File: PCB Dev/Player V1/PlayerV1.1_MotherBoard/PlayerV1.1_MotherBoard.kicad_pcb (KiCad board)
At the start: 2 copper layers, 64.3 x 83.5 mm, 66 parts, among them J1 USB_C_Receptacle_USB2.0, J3 SJ-3524-SMT-BE, U1 MIC5213-2.5YC5-TR, U2 TP4056, U3 AP7217A, U4 CP2102N-A02-GQFN28R, U5 BQ27441DRZR-G1A, U6 ESP32-WROOM-32E_(16MB), U7 MCP23017-E/ML

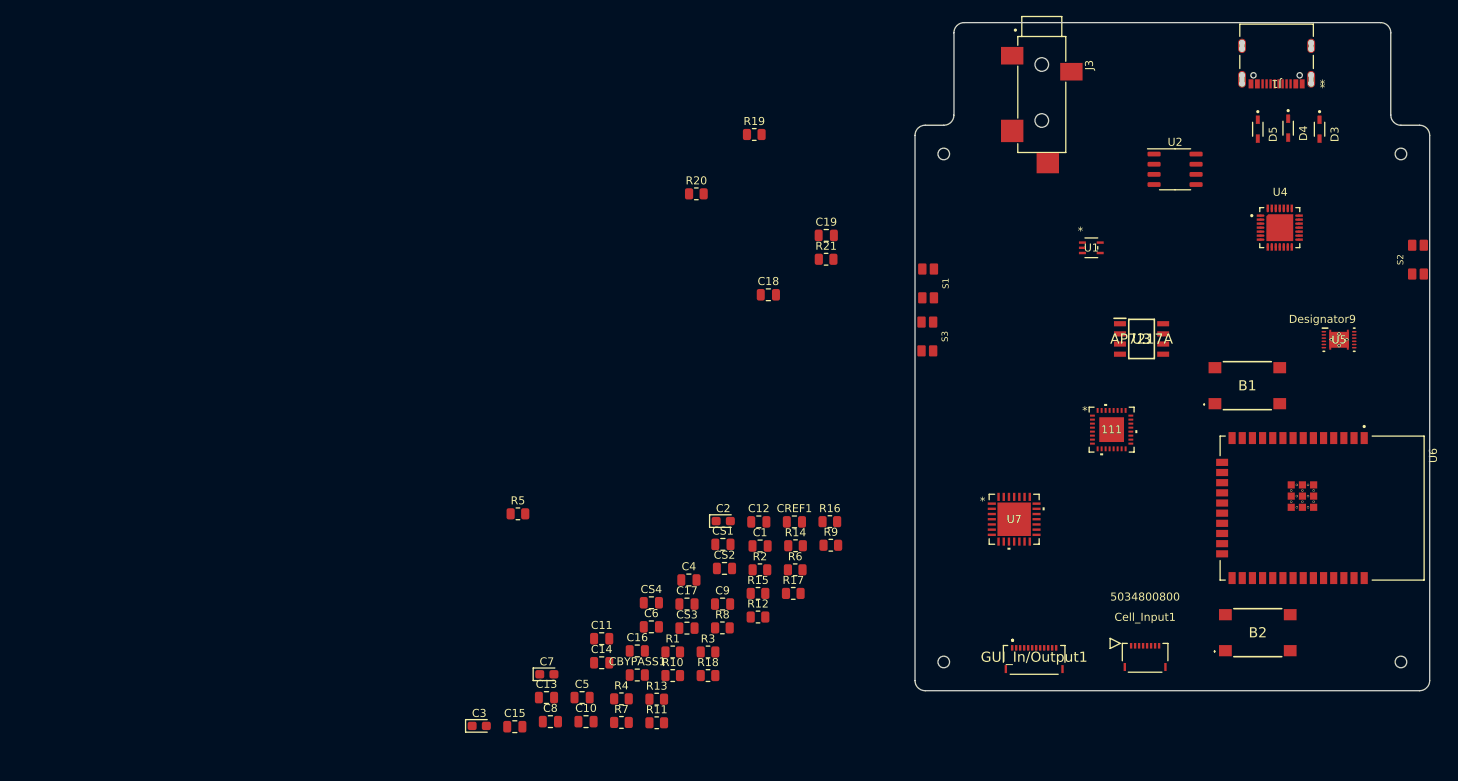
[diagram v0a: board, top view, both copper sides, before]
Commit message: added all jst connectors
new upward facing jst connectors
fixed footprint issue on the usbC port that resulted in a malformed board outline
need to add holes for the usbc port somehow
need to start laying out the pcb after using the component measurements to make proper pcb heights, cutouts, and tactile buttons
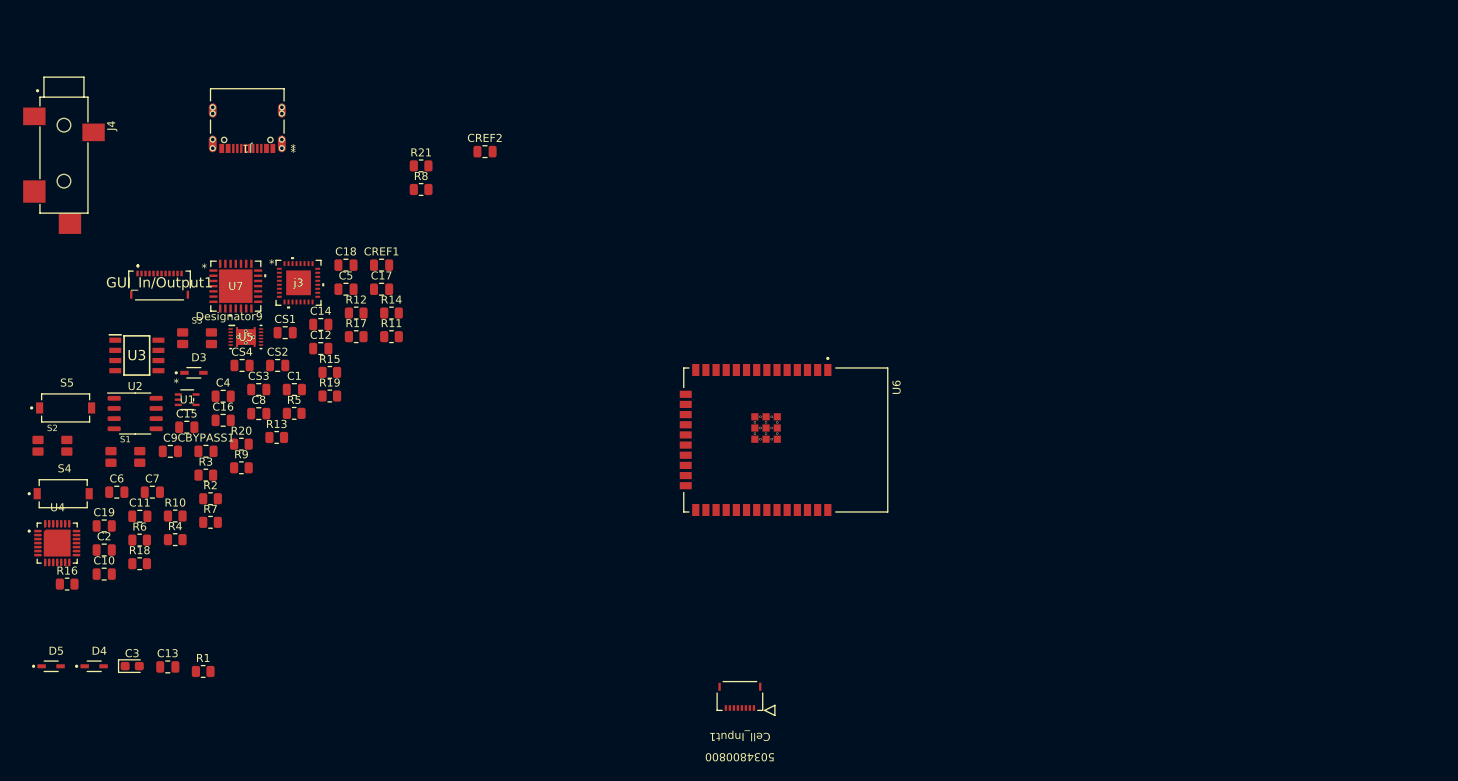
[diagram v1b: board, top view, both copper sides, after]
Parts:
- removed 111: LM49450SQ_NOPB, LM49450SQ_NOPB:SQA32A
- removed B1, B2: EVP-BT7A4A000, EVP-BT7A4A000:EVPBT7A4A000
- removed J3: SJ-3524-SMT-BE, SJ-3524-SMT-BE:CUI_SJ-3524-SMT-BE
- added CREF2: 0.1uF, Capacitor_SMD:C_0805_2012Metric, F.Cu at (110.9, 58.0)
- added J4: SJ-3524-SMT-BE, SJ-3524-SMT-BE:CUI_SJ-3524-SMT-BE, F.Cu at (58.2, 54.7)
- added S4: PTS636, PTS636_SM43J_SMTR_LFS:SW_PTS636_SM43J_SMTR_LFS, F.Cu at (58.1, 100.8)
- added S5: PTS636, PTS636_SM43J_SMTR_LFS:SW_PTS636_SM43J_SMTR_LFS, F.Cu at (58.4, 90.1)
- added j3: LM49450SQ_NOPB, LM49450SQ_NOPB:SQA32A, F.Cu at (87.6, 74.4)
- C19, CBYPASS1: value 1uF -> 2.2uF
- C2, C7: value 470nF -> 470uF; footprint Capacitor_Tantalum_SMD:CP_EIA-2012-15_AVX-P -> Capacitor_SMD:C_0805_2012Metric
- CREF1, CS2: value 1uF -> 10uF
- CS3: value 1uF -> 0.1uF
- moved S2 172.3 mm to (56.8, 94.8), turned to 0 degrees
- moved D5 165.1 mm to (56.6, 122.3), turned to 0 degrees
- moved D4 163.7 mm to (62.0, 122.3), turned to 0 degrees
- moved U4 157.8 mm to (57.4, 106.9)
- moved D3 144.0 mm to (74.5, 85.7), turned to 0 degrees
- moved U5 136.6 mm to (81.0, 81.2)
- moved U2 133.5 mm to (67.1, 90.8)
- moved J1 128.9 mm to (81.2, 53.9)
- moved U3 125.6 mm to (67.3, 83.5)
- moved GUI_In/Output1 118.9 mm to (70.2, 74.7)
- moved U1 114.6 mm to (73.6, 89.0)
- moved S1 102.7 mm to (65.9, 96.2), turned to 0 degrees
- moved U7 101.6 mm to (79.7, 74.8)
- moved C19 97.3 mm to (63.3, 104.8)
- moved R16 95.7 mm to (58.6, 112.1)
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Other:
- board outline removed

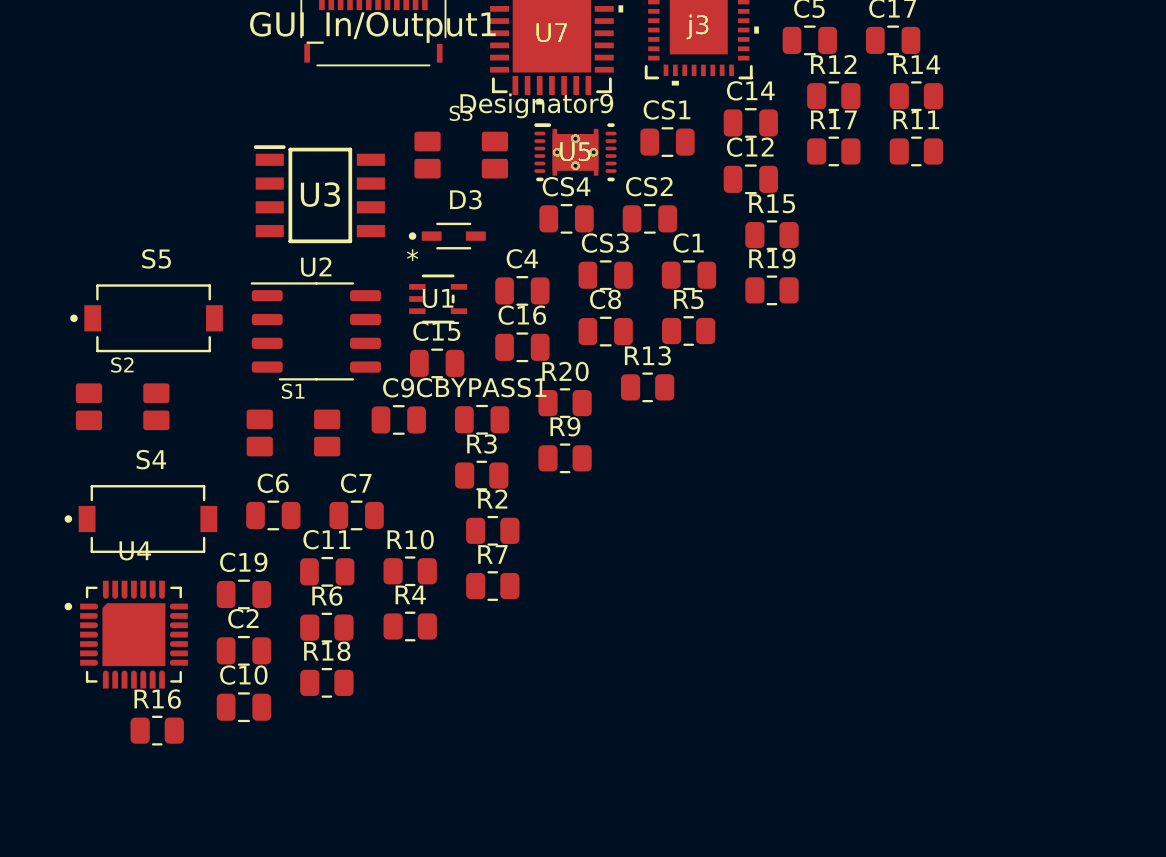
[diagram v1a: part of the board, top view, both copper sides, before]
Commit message: code
had to revise the code for the display and the audio so both can operate at the same time

using dma on both aspects already
dma on the display fixed it's operation issues
though dma was already in use on the i2s port and it was still stuttering so I have almost no official idea what the issue actually is
though, apparently the i2s amp i am currently using may be the issue so well have to make the official prototype then see
because then i wont have to worry about
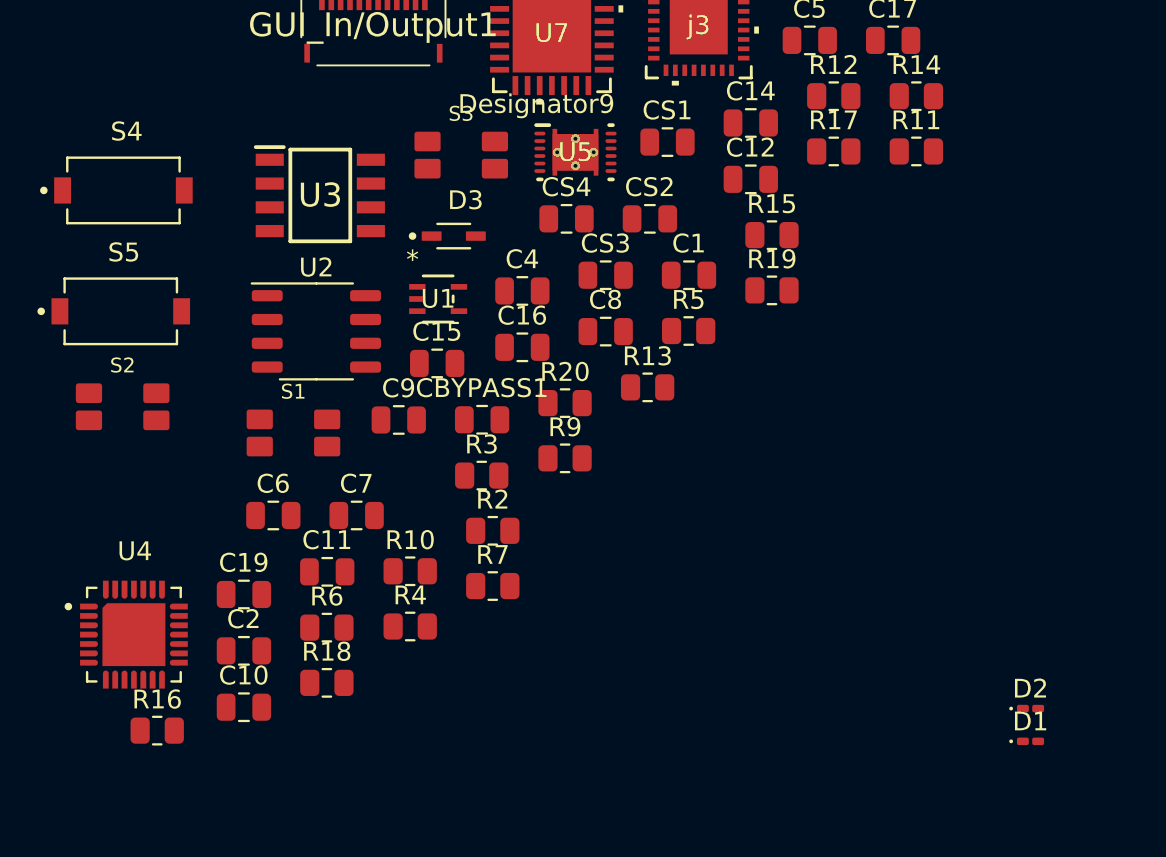
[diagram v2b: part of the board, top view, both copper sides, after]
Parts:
- added D1: LED, LED_SMD:LED_0201_0603Metric_Pad0.64x0.40mm_HandSolder, F.Cu at (105.3, 112.6)
- added D2: LED, LED_SMD:LED_0201_0603Metric_Pad0.64x0.40mm_HandSolder, F.Cu at (105.3, 110.9)
- moved S4 17.6 mm to (56.8, 83.2)
- moved S5 1.79 mm to (56.7, 89.7)
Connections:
- Cell_Input1 pad 3: /VCS -> /VMOSI
- Cell_Input1 pad 4: /VCLK -> /VMISO
- Cell_Input1 pad 5: /VMOSI -> /VCLK
- Cell_Input1 pad 6: /VMISO -> /VCS
- GUI_In/Output1 pad 11: unconnected-(GUI_In/Output1-Pad11) -> GND
- GUI_In/Output1 pad 12: unconnected-(GUI_In/Output1-Pad12) -> VCC
